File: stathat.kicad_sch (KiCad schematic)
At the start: 44 parts, among them J1 Conn_01x01, J2 Conn_01x01, J3 Conn_01x01, J4 Raspberry_Pi_2_3, J5 Conn_01x01, J6 Conn_01x01, J7 Conn_01x01, J8 Conn_01x01, J9 Conn_01x01, U1 LTV-844S, U2 74HC14

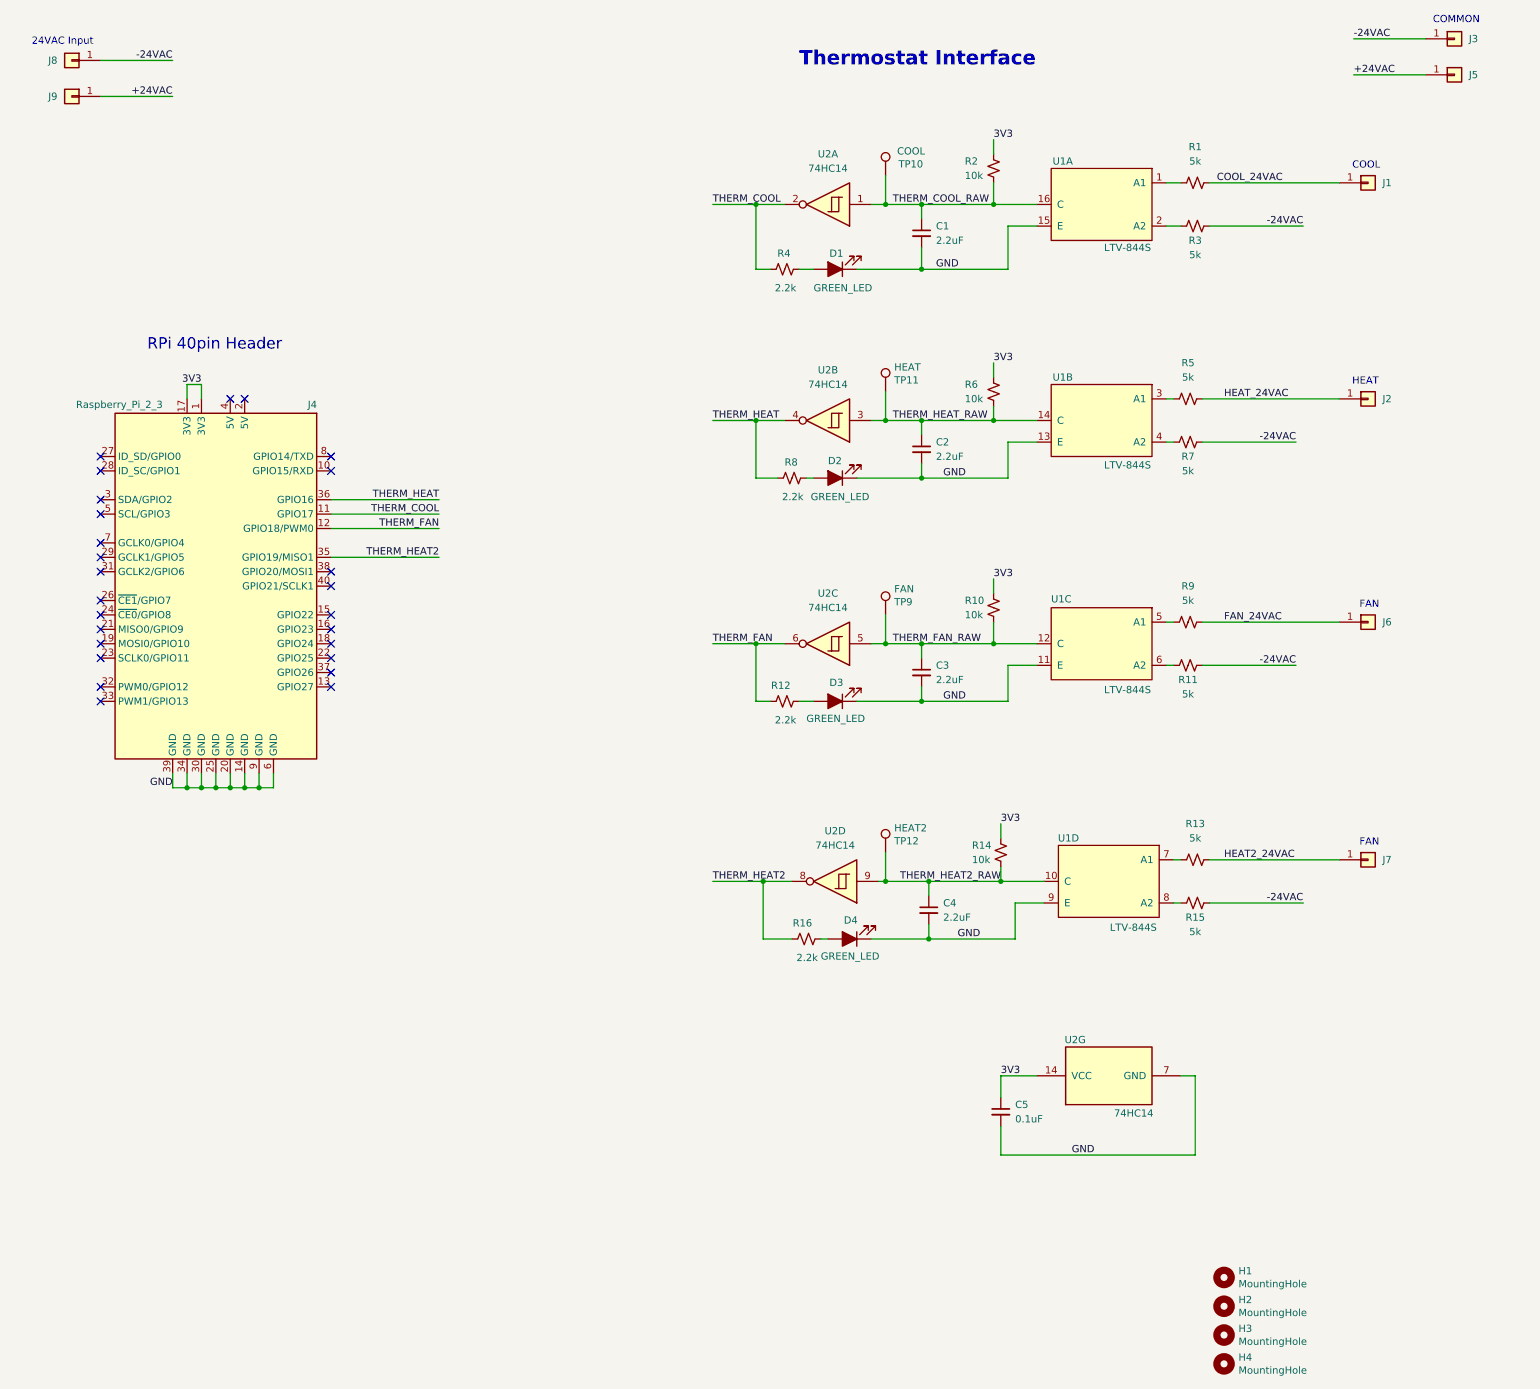
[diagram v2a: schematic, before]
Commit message: add fix for #1. move all vias out of pads. clean up traces. bump version number
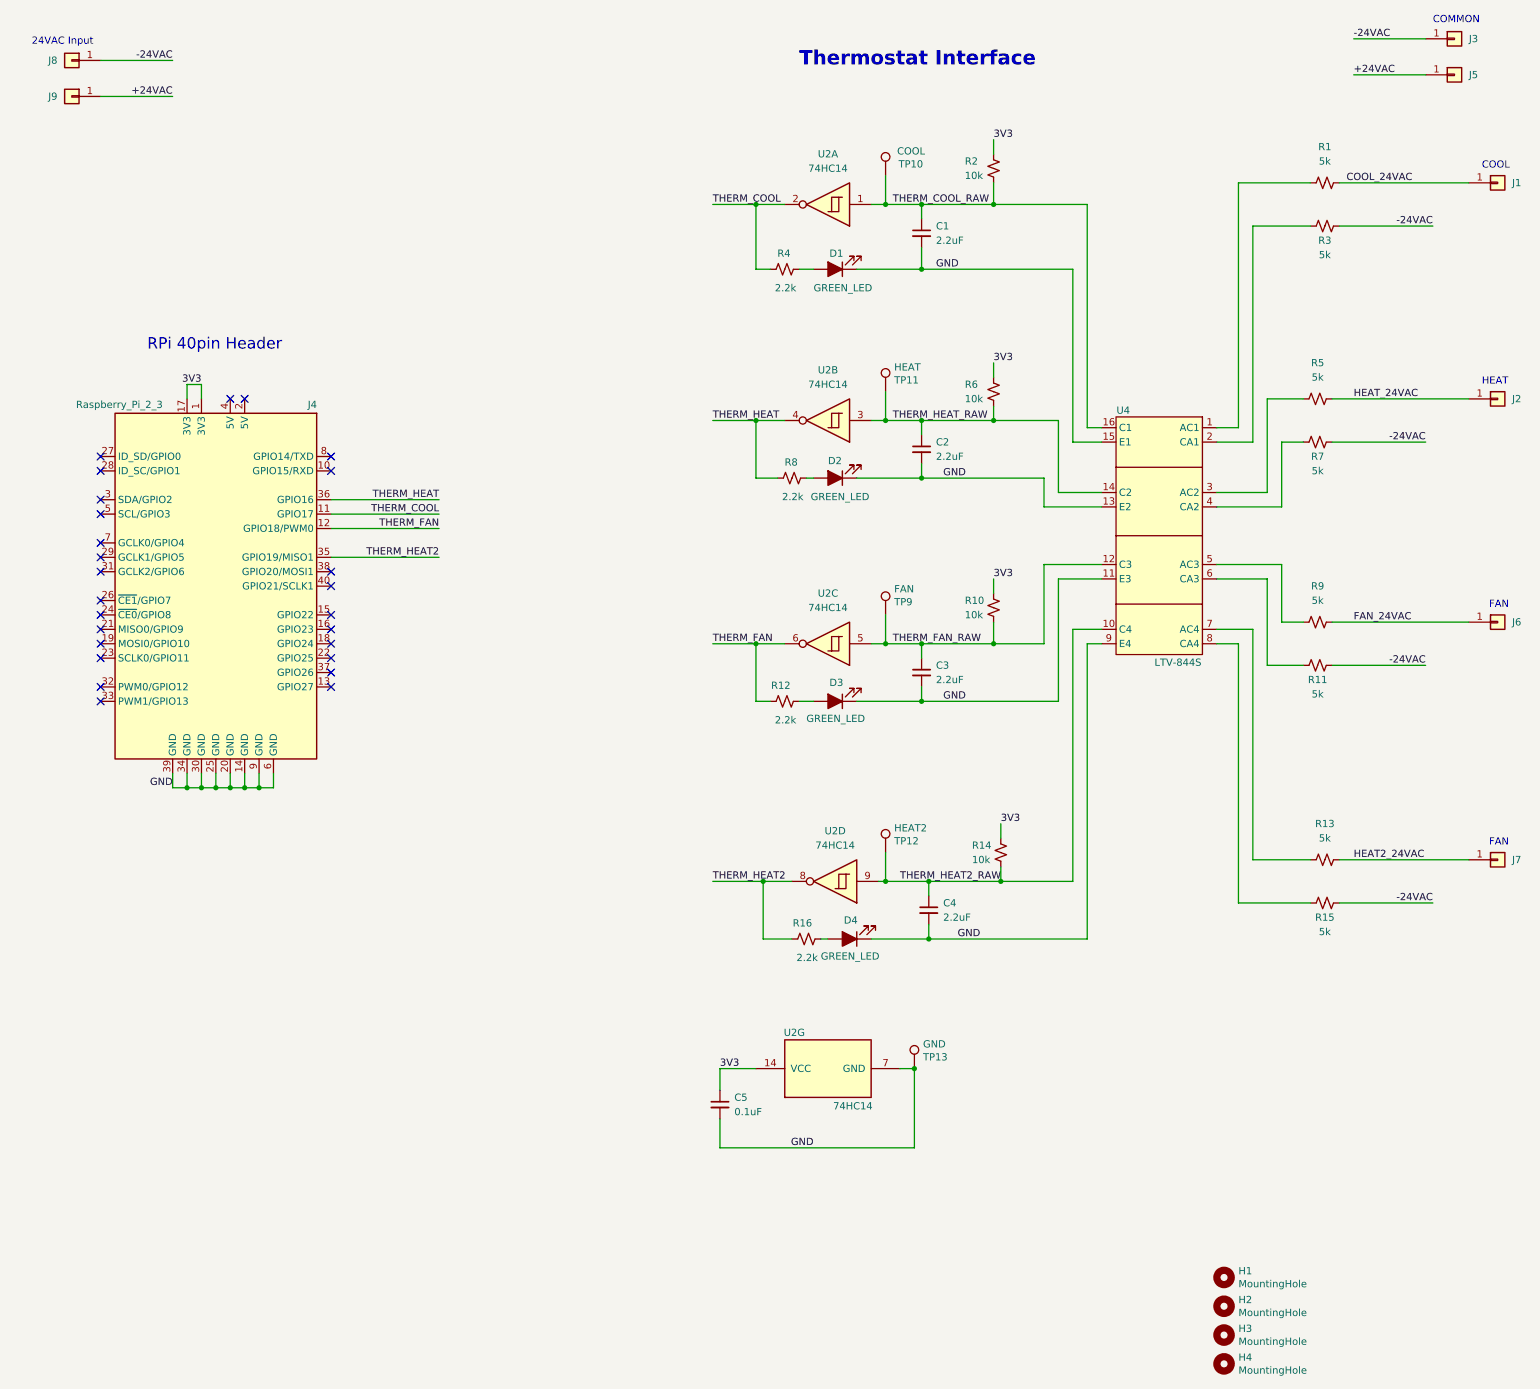
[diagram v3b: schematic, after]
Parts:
- removed U1: LTV-844S, Package_SO:SOIC-16W_7.5x10.3mm_P1.27mm, symbol stathat:LTV-844S
- added TP13: GND, stathat:TestPoint_Pad_D1.0mm, symbol Connector:TestPoint
- added U4: LTV-844S, stathat:OPTO-SMD-16_L19.8-W6.5-P2.54-LS10.2-BL, symbol stathat:LTV-844S
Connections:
- net GND: now also TP13.1, U4.11 (E3), U4.13 (E2), U4.15 (E1), U4.9 (E4)
- net THERM_COOL_RAW: now also U4.16 (C1)
- net THERM_FAN_RAW: now also U4.12 (C3)
- net THERM_HEAT2_RAW: now also U4.10 (C4)
- net THERM_HEAT_RAW: now also U4.14 (C2)
- net at R5.2: now also U4.3 (AC2)
- net at R11.2: now also U4.6 (CA3)
- net at R3.1: now also U4.2 (CA1)
- net at R9.2: now also U4.5 (AC3)
- net at R7.2: now also U4.4 (CA2)
- net at R15.2: now also U4.8 (CA4)
- net at R13.2: now also U4.7 (AC4)
- net at R1.2: now also U4.1 (AC1)
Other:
- moved on the sheet: C5, J1, J2, J6, J7, R1, R11, R13, R15, R3, R5, R7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
